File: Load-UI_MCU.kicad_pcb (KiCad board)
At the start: 4 copper layers, 85 x 90 mm, 111 parts, among them IC1 MSPM0G3519SPMR, IC2 TPS73533DRVT, IC3 TC4429CPA, J1 Conn_01x05_Socket, J10 Conn_01x02_Socket, J11 Conn_01x02_Socket, J12 Conn_01x02_Socket, J13 Conn_01x02_Socket, J14 Conn_01x02_Socket, J15 Conn_01x08_Pin, J16 Conn_01x02_Socket, J19 Conn_01x03_Socket, J2 Conn_01x06_Socket, J20 Conn_01x02_Socket, J21 Conn_01x02_Socket, J22 Conn_01x02_Socket, J23 Conn_01x02_Socket, J24 Conn_01x02_Socket, J3 Conn_01x02_Socket, J4 Conn_01x06_Socket, J5 Conn_01x02_Socket, J6 Conn_01x02_Socket, J7 Conn_01x02_Socket, J8 Conn_01x06_Socket, J9 Conn_01x03_Socket, Q2 2N2219, SW1 SW_Push, SW2 SW_Push, SW4 SW_Push_DPDT, U1 INA229AQDGSRQ1, U2 INA229AQDGSRQ1, U3 SN74HC14N

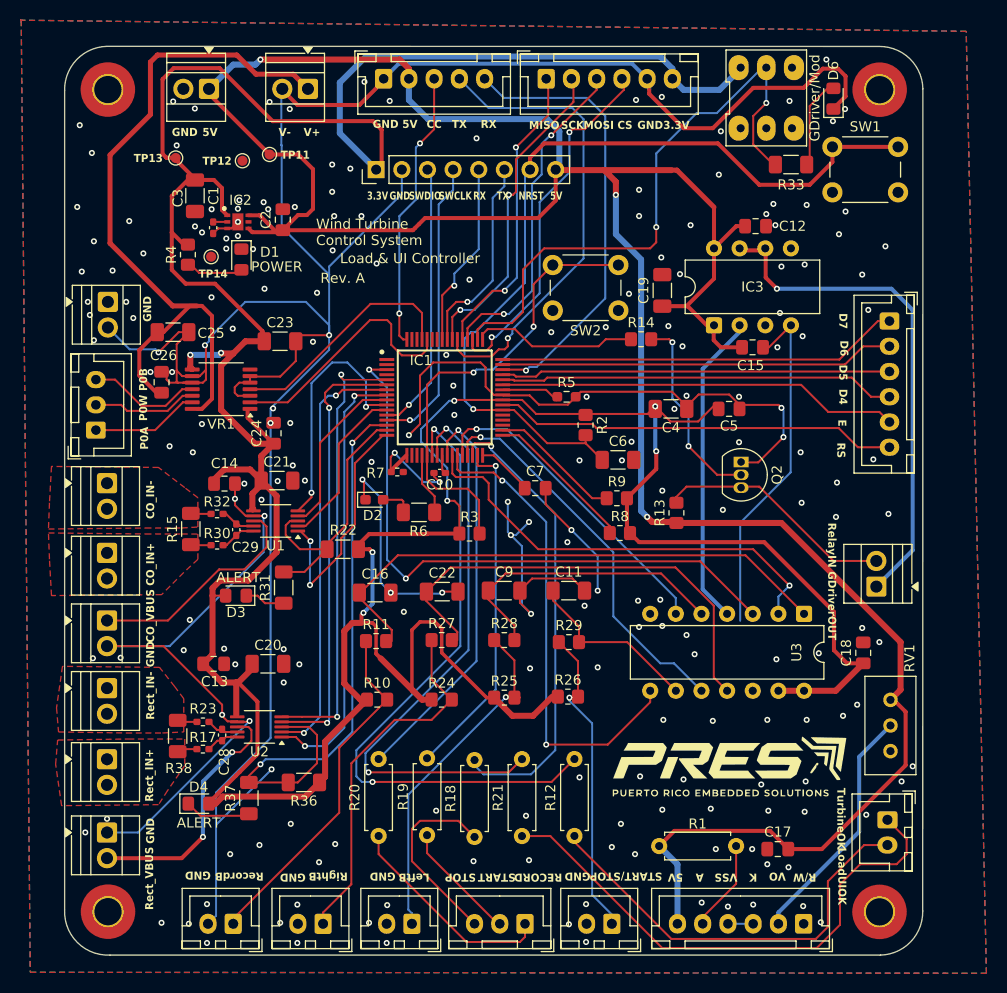
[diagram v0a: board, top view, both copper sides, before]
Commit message: added two more testpoints
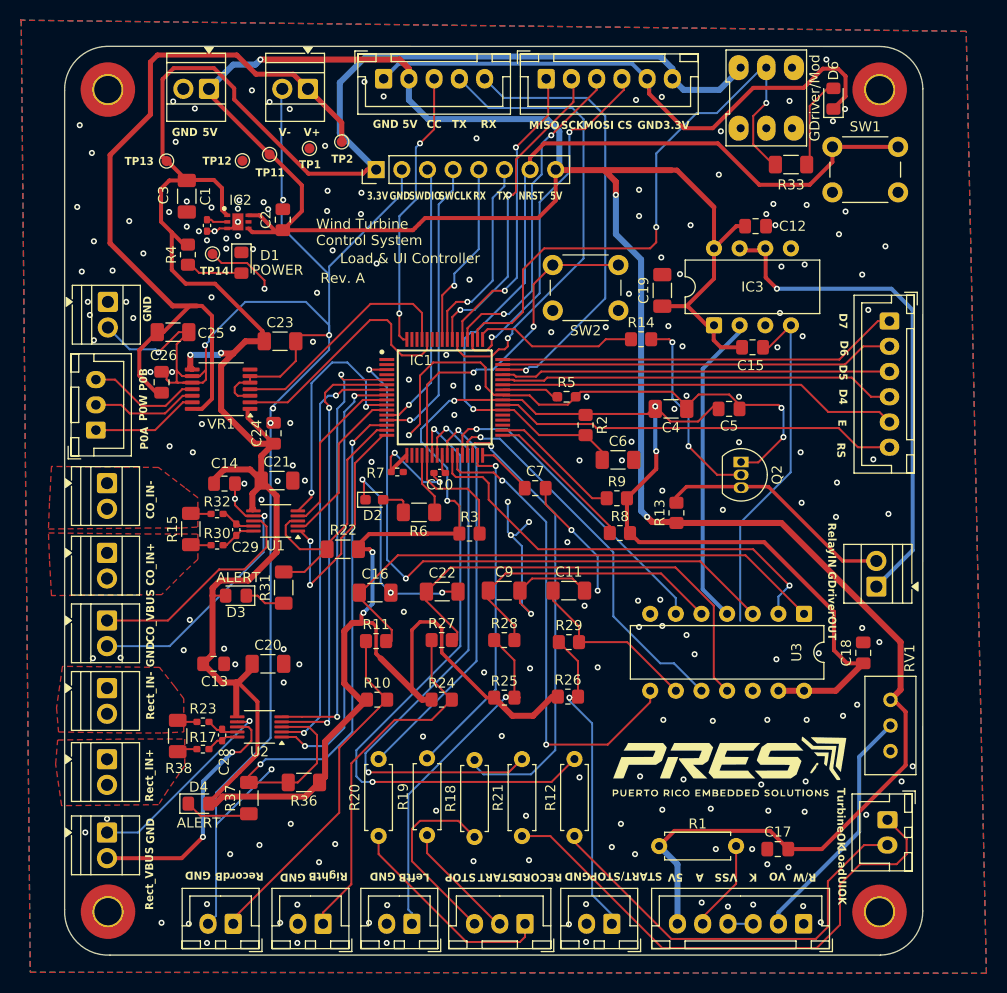
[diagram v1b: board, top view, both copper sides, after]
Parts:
- added TP1: TestPoint, TestPoint:TestPoint_Pad_D1.0mm, F.Cu at (141.2, 60.1)
- added TP2: TestPoint, TestPoint:TestPoint_Pad_D1.0mm, F.Cu at (144.4, 59.5)
- R13: value 220 -> 1k
- moved TP13 0.95 mm to (127.1, 61.4)
- moved C1 0.81 mm to (129.1, 64.8)
- moved C3 0.65 mm to (131.1, 67.7)
- moved D1 0.33 mm to (134.5, 71.4)
- moved TP14 0.31 mm to (131.7, 70.5)
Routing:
- net GND: track 459.3 -> 438.4 mm, vias 210 -> 219
- net External_Power_Supply: track 73.2 -> 79.8 mm
- net +5V: track 265.8 -> 262.8 mm
- net Net-(IC2-NR): track 1.41 -> 2.10 mm

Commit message: PCB finished, only final manufacturing files left, BOM, CPL
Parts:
- added G***: LOGO, LOGO, F.Cu at (154.7, 84.8)
- R8, R9: value 1k -> 4.7k
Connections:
- IC1 pad 35: unconnected-(IC1-PA28-Pad35) -> UART0_TX_XDS
- IC1 pad 55: SD_SCK -> unconnected-(IC1-PA9_/_RTC_OUT_/_CLK_OUT-Pad55)
- IC1 pad 56: UART0_TX_XDS -> SD_SCK
- VR1 pad 7: unconnected-(VR1-NC-Pad7) -> GND
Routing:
- net UART0_TX_XDS: track 20.0 -> 32.2 mm
- net GND: vias 219 -> 221

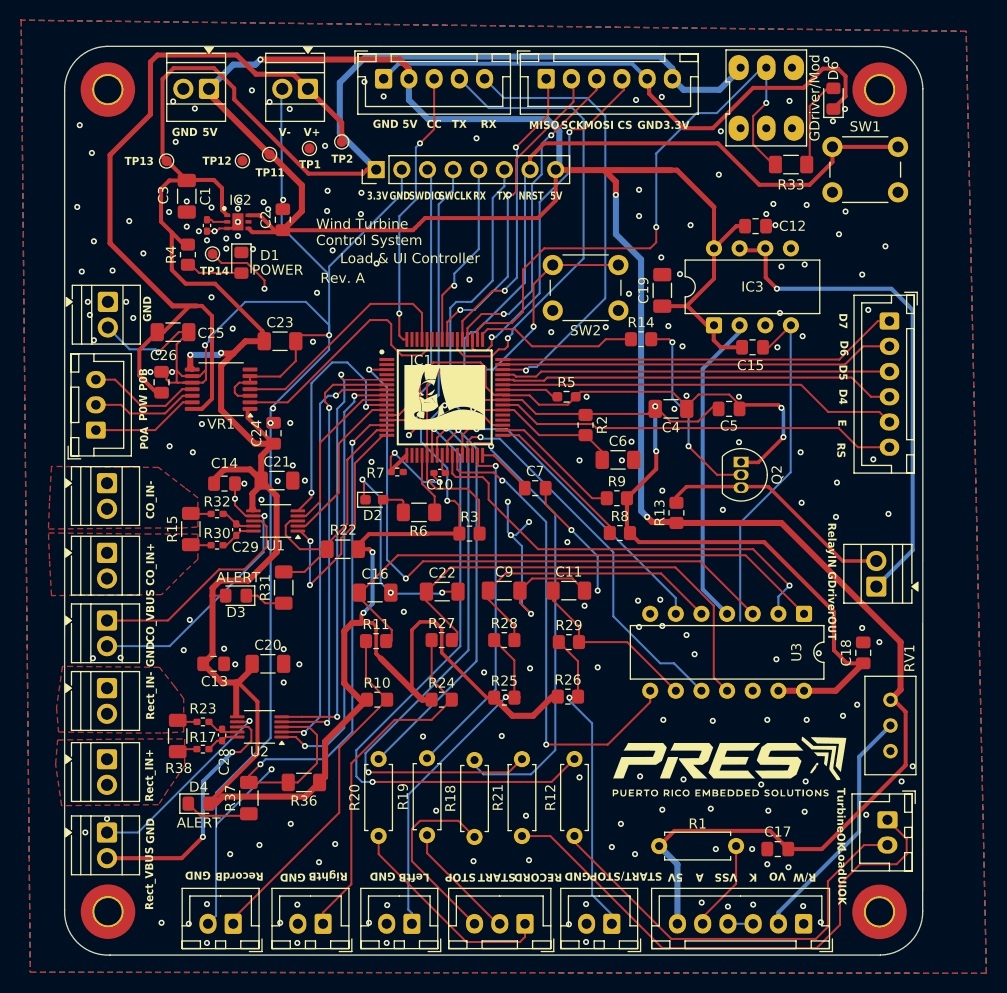
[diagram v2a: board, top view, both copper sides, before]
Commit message: This commit contains all files up dote to Rev A. Load & UI MCU, manufactured on May 21, 2026
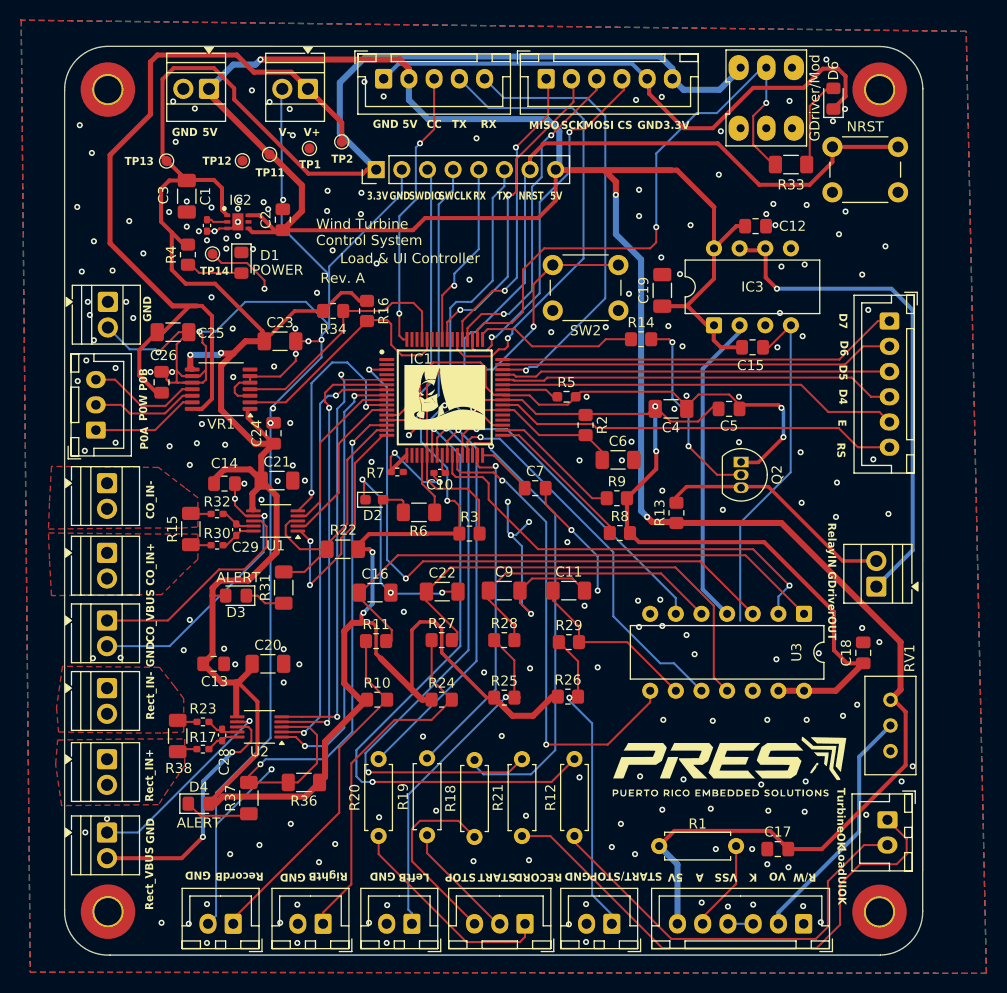
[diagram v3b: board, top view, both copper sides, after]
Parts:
- added R16: 4.7k, Resistor_SMD:R_0805_2012Metric_Pad1.20x1.40mm_HandSolder, F.Cu at (146.9, 76.2)
- added R34: 4.7k, Resistor_SMD:R_0805_2012Metric_Pad1.20x1.40mm_HandSolder, F.Cu at (143.6, 76.2)
- renumbered SW1 to NRST
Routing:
- net +3.3V: track 403.7 -> 416.2 mm
- net SDA: track 23.5 -> 24.9 mm
- net GND: track 438.4 -> 437.9 mm, vias 221 -> 233
